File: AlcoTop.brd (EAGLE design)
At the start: 44.1 x 58.4 mm, 27 parts, among them IC4 ATMEGA328, Y1 16MHz

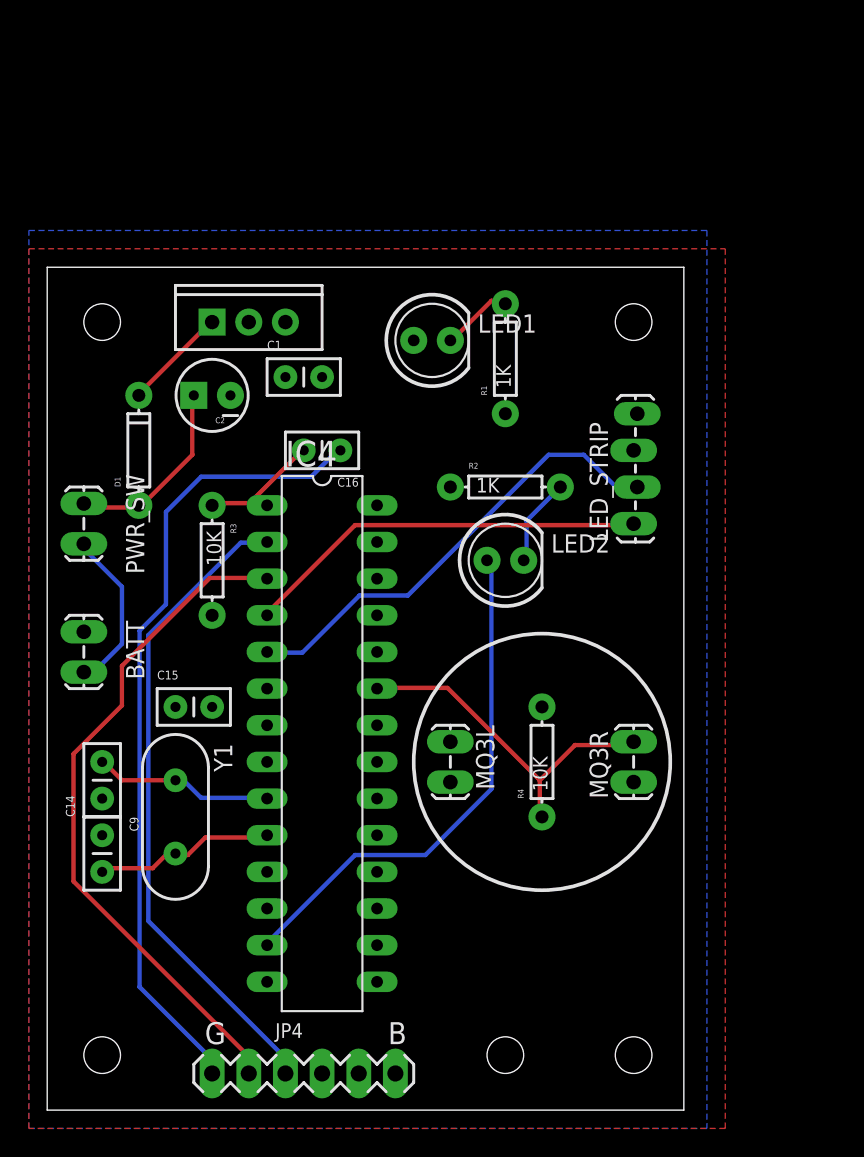
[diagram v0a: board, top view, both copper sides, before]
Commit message: Added transistor switch for MQ3 and pushbutton to change mode. 100mA operating current. YAY
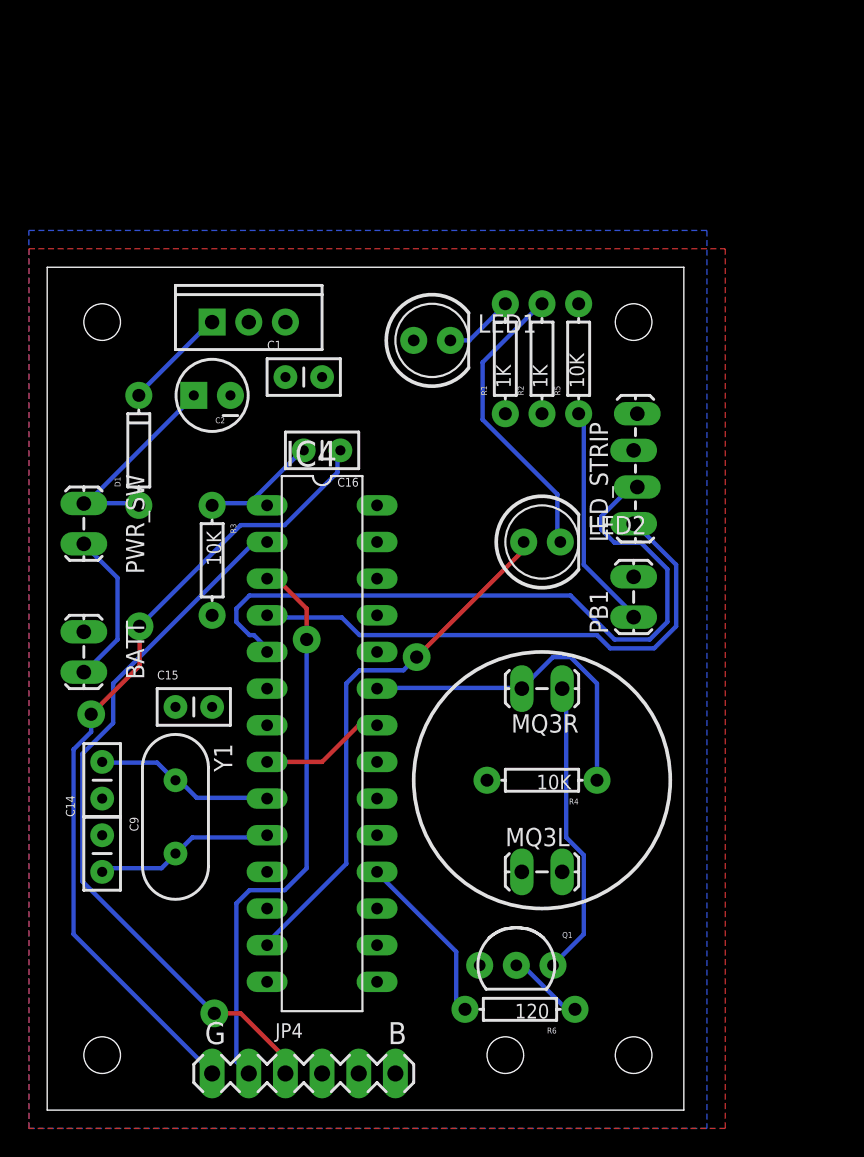
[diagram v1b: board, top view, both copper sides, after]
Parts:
- added PB1: (no value), SparkFun-Connectors:1X02_LOCK_LONGPADS
- added Q1: (no value), SparkFun-DiscreteSemi:TO-92-AMMO
- added R5: 10K, Dek:AXIAL-0.3
- added R6: 120, Dek:AXIAL-0.3
- moved MQ3L 10.2 mm to (33.0, 16.5), turned to 0 degrees
- moved R2 9.25 mm to (34.3, 52.1), turned to 90 degrees
- moved MQ3R 8.13 mm to (35.6, 29.2), turned to 180 degrees
- moved LED2 2.84 mm to (34.3, 39.4)
- moved R4 1.27 mm to (34.3, 22.9), turned to 180 degrees
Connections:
- new net MQ3: MQ3R.1, Q1.3
- new net N$5: IC4.28
- new net N$7: Q1.2, R6.P$1
- net D12: now also R6.P$2
- net GND: now also Q1.1, R5.P$2; no longer MQ3R.1
- net SCL: now also PB1.1, R5.P$1; no longer IC4.28
- net VCC: now also PB1.2
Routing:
- net MQ3: track 0.00 -> 20.7 mm
- net D3: track 32.3 -> 49.8 mm
- net SCL: track 0.00 -> 15.6 mm
- net N$4: track 6.25 -> 20.5 mm
- net D12: track 0.00 -> 12.1 mm
- net D2: track 28.1 -> 38.4 mm
- net GND: track 0.00 -> 8.67 mm
- net TX: track 47.3 -> 39.8 mm, vias 0 -> 1
- net N$7: track 0.00 -> 5.42 mm
- net RX: track 45.2 -> 49.6 mm, vias 0 -> 1
- net DTR: track 55.6 -> 56.7 mm, vias 0 -> 2
- net D7: track 36.1 -> 37.1 mm, vias 0 -> 1
- net N$3: track 13.5 -> 14.4 mm
- net N$2: track 11.5 -> 10.8 mm
- net A0: track 24.3 -> 23.7 mm

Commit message: Updated board
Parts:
- removed JP5: STAND-OFF#2, Dek:STAND-OFF-#2
- removed PB1: (no value), SparkFun-Connectors:1X02_LOCK_LONGPADS
- added MODE: (no value), Dek:1X02_LOCK_LONGPADS
- BATT, MQ3L, MQ3R, PWR_SW: device SparkFun-Connectors:1X02_LOCK_LONGPADS -> Dek:1X02_LOCK_LONGPADS
- D1: value (none) -> 1N4001; device Dek:DIODE-1N4148 -> Dek:DIODE-1N4001
- IC2: value (none) -> 7805; device SparkFun-PowerIC:TO220-IGO -> Dek:TO220-IGO
- IC4: device atmel:DIL28-3 -> Dek:DIL28-3
- LED1, LED2: device SparkFun-LED:LED5MM -> Dek:LED5MM
- LED_STRIP: device SparkFun-Connectors:1X04_LOCK_LONGPADS -> Dek:1X04_LOCK_LONGPADS
- Y1: device SparkFun:HC49US -> Dek:HC49US
- moved R5 39.6 mm to (7.62, 25.4)
- moved C9 39.2 mm to (38.1, 38.1), turned to 180 degrees
- moved C16 37.0 mm to (6.35, 11.4), turned to 90 degrees
- moved Y1 33.3 mm to (34.3, 41.9), turned to 0 degrees
- moved C14 31.4 mm to (30.5, 38.1), turned to 0 degrees
- moved R2 30.5 mm to (35.6, 21.6), turned to 180 degrees
- moved IC4 26.9 mm to (27.9, 50.8), turned to 0 degrees
- moved R3 25.5 mm to (8.89, 12.7)
- moved C15 23.4 mm to (26.7, 43.2), turned to 270 degrees
- moved Q1 22.9 mm to (48.3, 26.7), turned to 90 degrees
- moved LED2 21.8 mm to (21.6, 21.6)
- moved R1 19.1 mm to (43.2, 67.3)
- moved JP1 18.8 mm to (49.5, 71.1)
- moved LED1 18.1 mm to (38.1, 67.3)
- moved D1 17.8 mm to (7.62, 63.5)
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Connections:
- removed net SCL: PB1.1, R5.P$1
- net D2: now also MODE.1, R5.P$1; no longer LED_STRIP.1
- net D3: now also LED2.A; no longer LED_STRIP.2
- net D7: now also LED_STRIP.1; no longer LED2.A
- net D8: now also LED_STRIP.2
- net VCC: now also MODE.2; no longer PB1.2
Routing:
- net DTR: track 56.7 -> 13.5 mm, vias 2 -> 0
- net D12: track 12.1 -> 43.2 mm
- net RST: track 10.5 -> 35.5 mm
- net D3: track 49.8 -> 26.1 mm
- net D7: track 37.1 -> 15.6 mm, vias 1 -> 0
- net SCL: track 15.6 -> 0.00 mm
- net A0: track 23.7 -> 38.1 mm
- net N$7: track 5.42 -> 19.8 mm
- net D8: track 0.00 -> 12.6 mm
- net N$4: track 20.5 -> 9.08 mm
- net MQ3: track 20.7 -> 11.9 mm
- net GND: track 8.67 -> 0.00 mm
- net RX: track 49.6 -> 43.1 mm
- net D2: track 38.4 -> 34.9 mm
- net TX: track 39.8 -> 43.2 mm
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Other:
- board size 44.1 x 58.4 mm -> 51.7 x 73.7 mm
- board text added: "AlcoTop v1.0"
- board text added: "Jan 2013"

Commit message: Reduced MQ3 voltage divider resistor to 1K
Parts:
- R4: value 10K -> 1K
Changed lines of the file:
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@@
 <setting verticaltext="up"/>
 </settings>
-<grid distance="0.05" unitdist="inch" unit="mm" style="lines" multiple="1" display="yes" altdistance="0.005" altunitdist="inch" altunit="inch"/>
+<grid distance="0.05" unitdist="inch" unit="inch" style="lines" multiple="1" display="yes" altdistance="0.005" altunitdist="inch" altunit="inch"/>
 <layers>
 <layer number="1" name="Top" color="4" fill="1" visible="yes" active="yes"/>
@@
 <attribute name="VALUE" x="38.1" y="31.242" size="1.27" layer="27" font="vector" rot="R180"/>
 </element>
-<element name="R4" library="Dek" package="AXIAL-0.3" value="10K" x="35.56" y="24.13" smashed="yes" rot="R180">
+<element name="R4" library="Dek" package="AXIAL-0.3" value="1K" x="35.56" y="24.13" smashed="yes" rot="R180">
 <attribute name="NAME" x="38.1" y="22.86" size="0.4064" layer="25" font="vector" rot="R180"/>
 <attribute name="VALUE" x="37.084" y="24.638" size="1.016" layer="21" font="vector" rot="R180"/>
